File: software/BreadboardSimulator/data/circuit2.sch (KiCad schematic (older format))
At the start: 8 parts, among them Q1 Transistor, U1-8 8pinChip

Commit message: modify scale of prefabs
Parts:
- added GND, GND1, GND2, GND3: GND, symbol SchemaBoard_Library:GND
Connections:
- net GND: now also GND.1 (GND), GND1.1 (GND), GND2.1 (GND), GND3.1 (GND)
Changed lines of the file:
@@
 $EndComp
 $Comp
-L SchemaBoard_Library:GND #PWR0101
+L SchemaBoard_Library:GND GND2
 U 1 1 5D3D0435
 P 5050 5700
-F 0 "#PWR0101" H 5050 5450 50  0001 C CNN
+F 0 "GND2" H 5050 5450 50  0001 C CNN
 F 1 "GND" H 5055 5527 50  0000 C CNN
 F 2 "" H 5050 5700 50  0001 C CNN
@@
 $EndComp
 $Comp
-L SchemaBoard_Library:GND #PWR0102
+L SchemaBoard_Library:GND GND
 U 1 1 5D3D0965
 P 7900 2100
-F 0 "#PWR0102" H 7900 1850 50  0001 C CNN
+F 0 "GND" H 7900 1850 50  0001 C CNN
 F 1 "GND" H 7905 1927 50  0000 C CNN
 F 2 "" H 7900 2100 50  0001 C CNN
@@
 	5050 4700 5050 5700
 $Comp
-L SchemaBoard_Library:GND #PWR0103
+L SchemaBoard_Library:GND GND1
 U 1 1 5D3F22A2
 P 6350 5700
-F 0 "#PWR0103" H 6350 5450 50  0001 C CNN
+F 0 "GND1" H 6350 5450 50  0001 C CNN
 F 1 "GND" H 6355 5527 50  0000 C CNN
 F 2 "" H 6350 5700 50  0001 C CNN
@@
 	6350 5000 6350 5700
 $Comp
-L SchemaBoard_Library:GND #PWR0104
+L SchemaBoard_Library:GND GND3
 U 1 1 5D3FA6A0
 P 4500 6950
-F 0 "#PWR0104" H 4500 6700 50  0001 C CNN
+F 0 "GND3" H 4500 6700 50  0001 C CNN
 F 1 "GND" H 4505 6777 50  0000 C CNN
 F 2 "" H 4500 6950 50  0001 C CNN

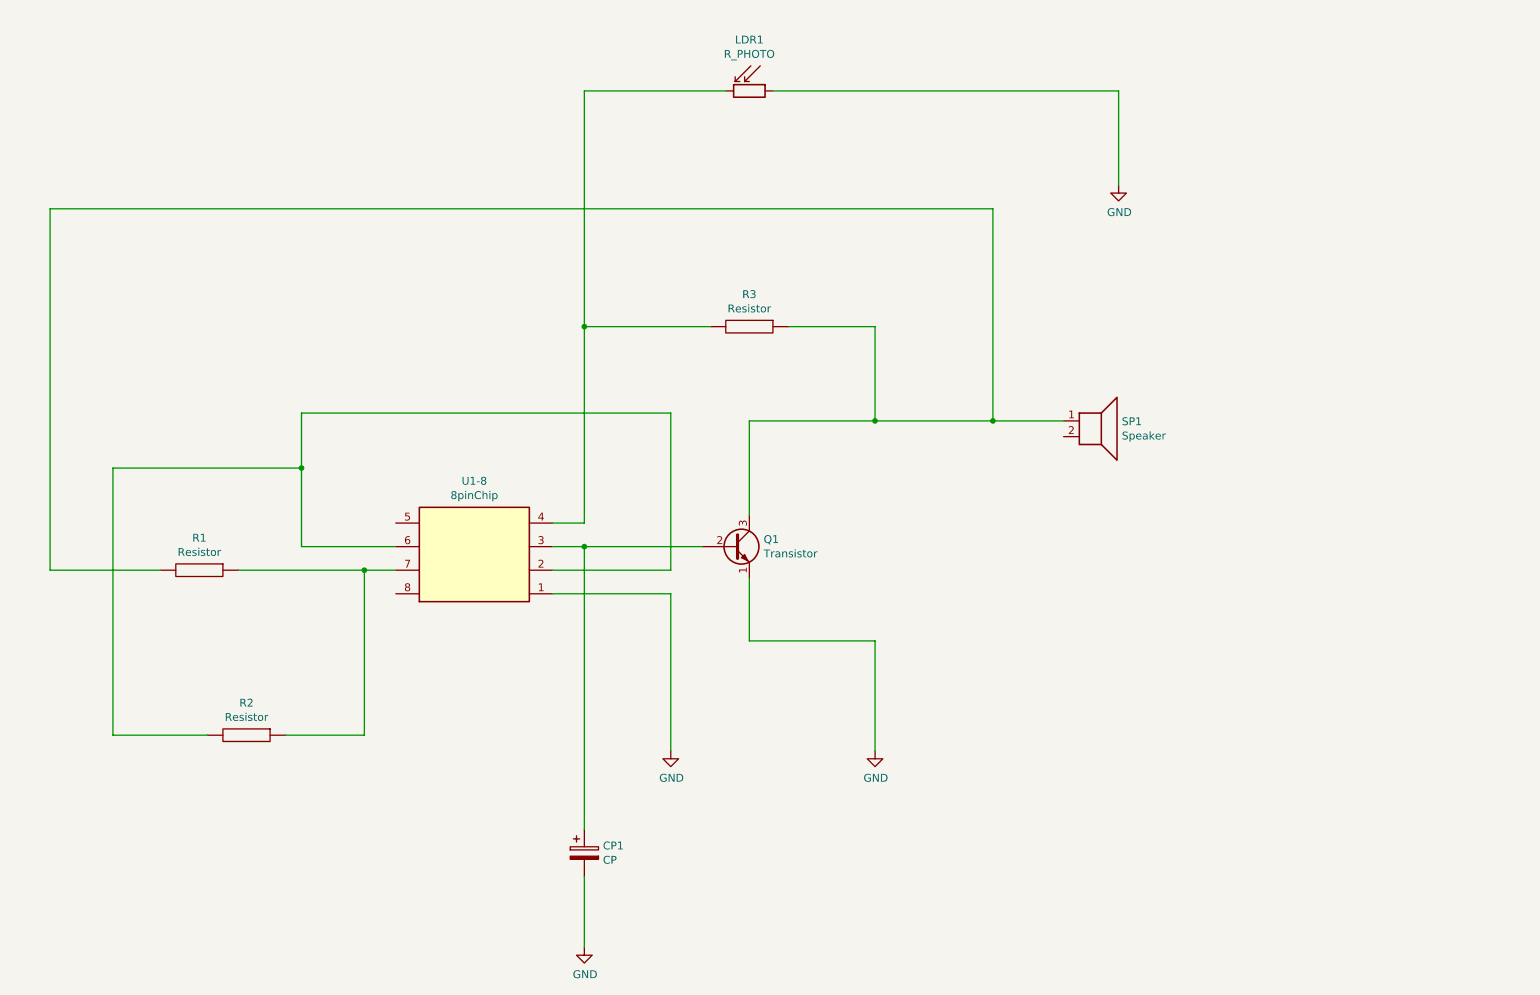
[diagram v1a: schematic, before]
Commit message: resize button for prefabs
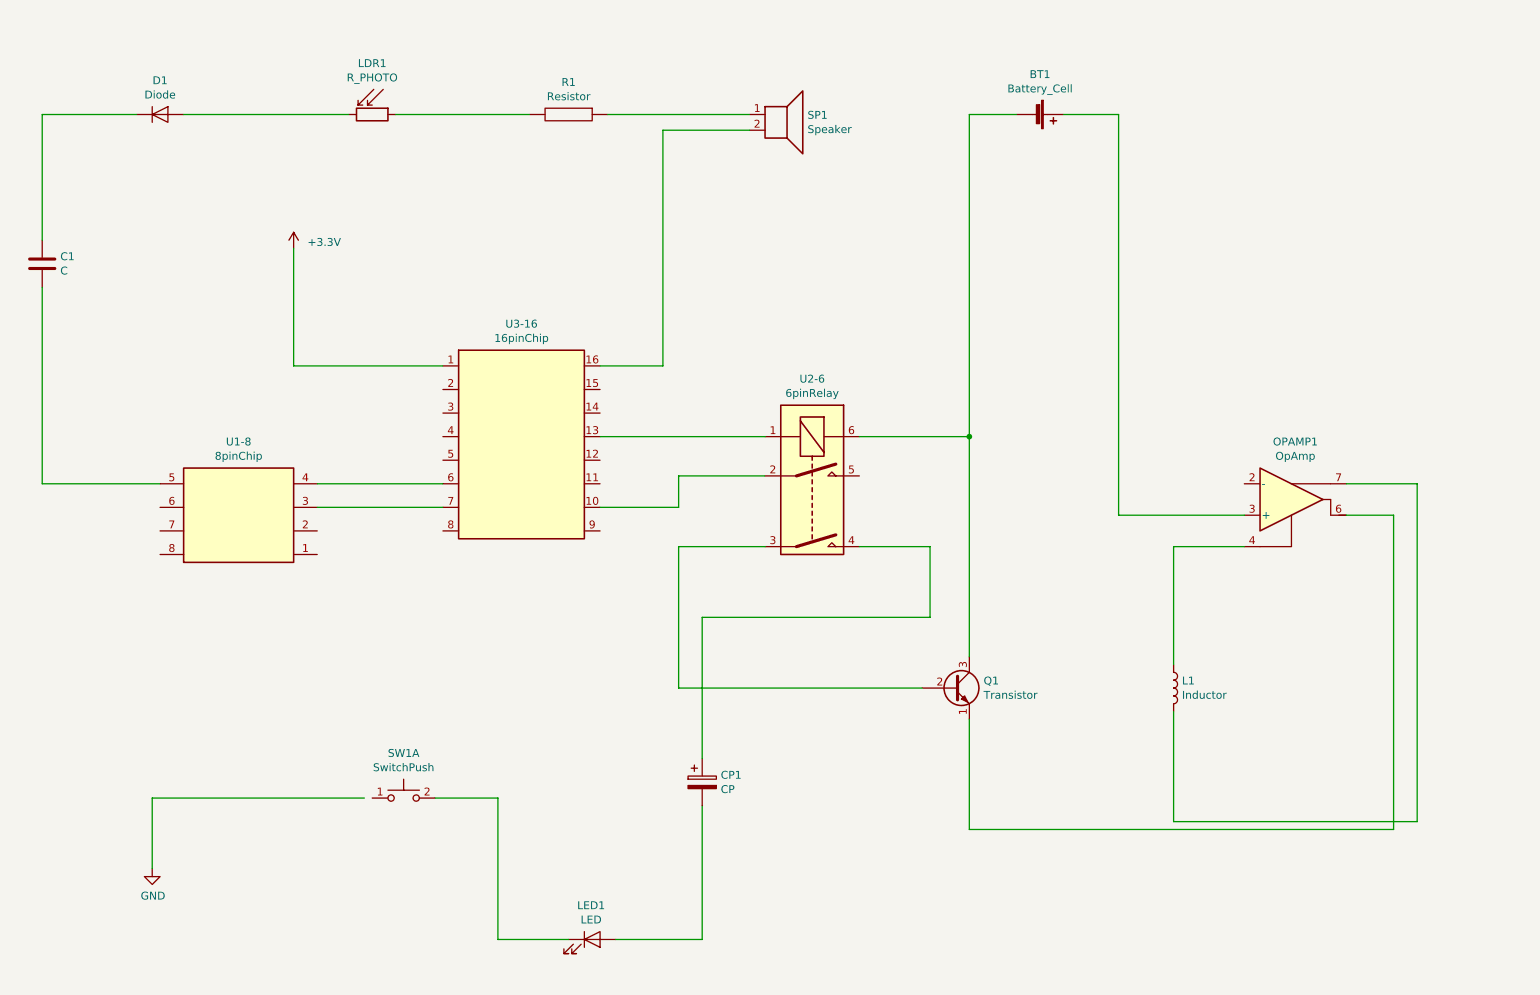
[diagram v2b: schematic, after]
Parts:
- removed GND1, GND2, GND3: GND, symbol SchemaBoard_Library:GND
- removed R1, R2: Resistor, symbol SchemaBoard_Library:Resistor
- added BT1: Battery_Cell, symbol SchemaBoard_Library:Battery_Cell
- added C1: C, symbol SchemaBoard_Library:C
- added D1: Diode, symbol SchemaBoard_Library:Diode
- added L1: Inductor, symbol SchemaBoard_Library:Inductor
- added LED1: LED, symbol SchemaBoard_Library:LED
- added OPAMP1: OpAmp, symbol SchemaBoard_Library:OpAmp
- added PWR1: +3.3V, symbol SchemaBoard_Library:+3.3V
- added SW1: SwitchPush, symbol SchemaBoard_Library:SwitchPush
- added U2-6: 6pinRelay, Relay_THT, symbol SchemaBoard_Library:6pinRelay
- added U3-16: 16pinChip, symbol SchemaBoard_Library:16pinChip
- renumbered GND to GND1, R3 to R1
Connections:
- net GND: no longer CP1.2, LDR1.1, Q1.1 (E), U1-8.1
- net at U1-8.2: no longer U1-8.6
- net at U1-8.5: now also C1.2
- net at R1.1, SP1.1: no longer Q1.3 (C)
- net at SP1.2: now also U3-16.16
- new net: U1-8.3, U3-16.7
- new net: U1-8.4, U3-16.6
- new net: LDR1.1, R1.2
- new net: D1.2 (A), LDR1.2
- new net: OPAMP1.6, Q1.1 (E)
- new net: Q1.2 (B), U2-6.3
- new net: BT1.2 (-), Q1.3 (C), U2-6.6
- new net: U2-6.1, U3-16.13
- new net: U2-6.2, U3-16.10
- new net: CP1.1, U2-6.4
- new net: C1.1, D1.1 (K)
- new net: L1.1, OPAMP1.4
- new net: L1.2, OPAMP1.7
- new net: LED1.1 (K), SW1.2 (D)
- new net: CP1.2, LED1.2 (A)
- new net: BT1.1 (+), OPAMP1.3 (+)
- new net +3V3: PWR1.1 (+3V3), U3-16.1
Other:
- moved on the sheet: CP1, LDR1, Q1, R1, SP1, U1-8

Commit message: Recover initial position if the user changes mode with disconnected components
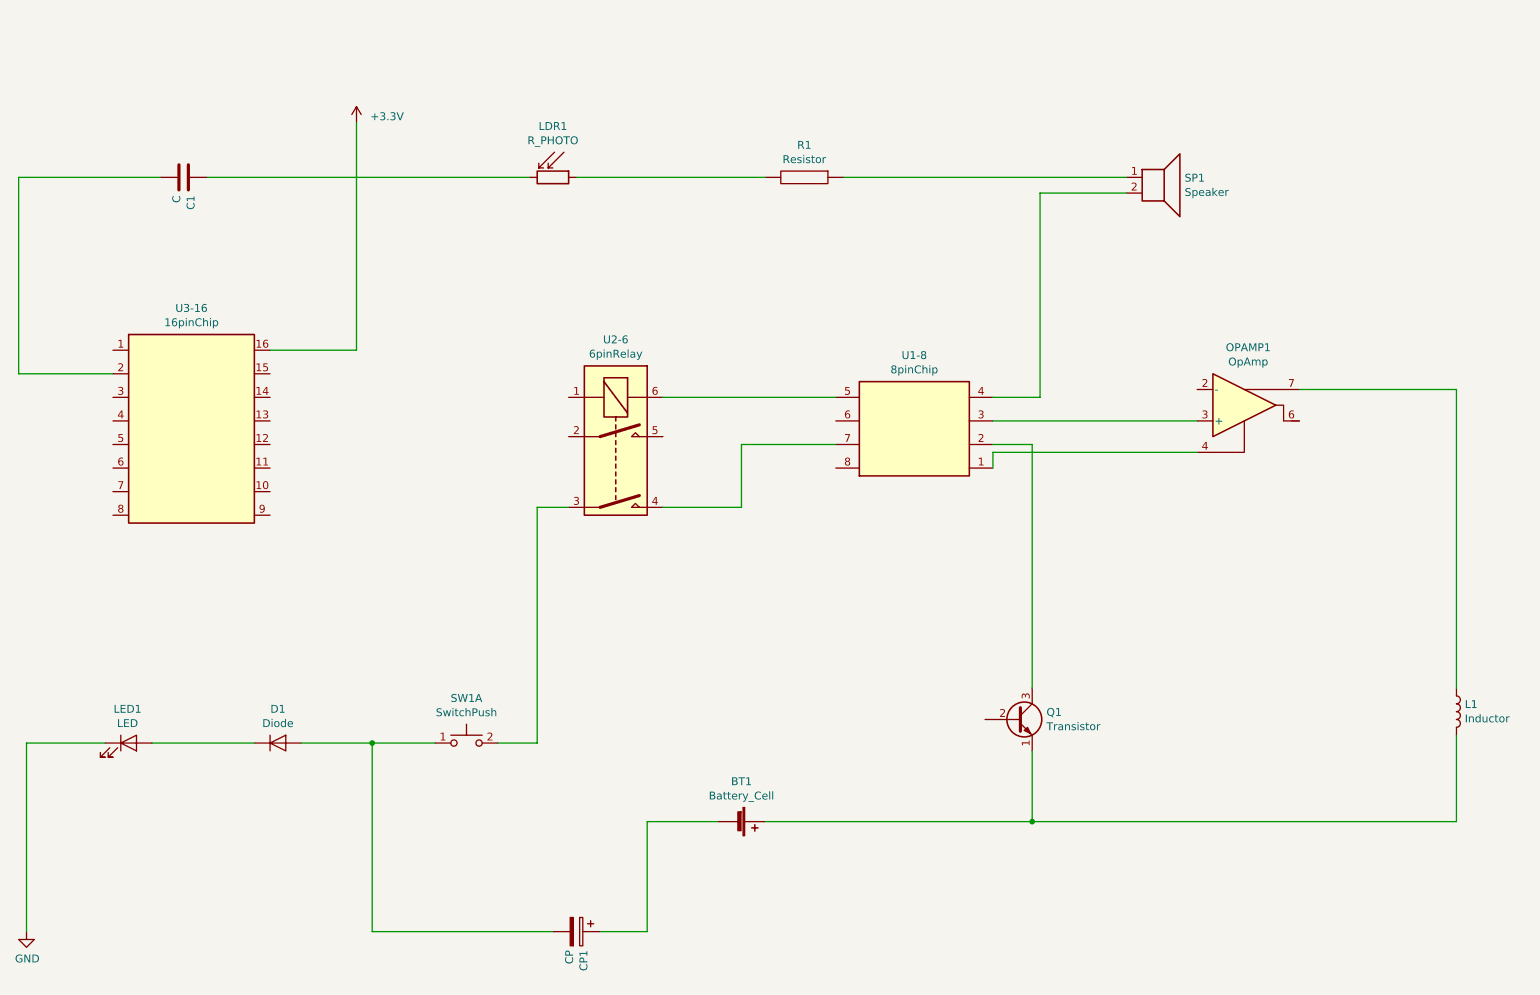
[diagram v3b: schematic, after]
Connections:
- net +3V3: now also U3-16.16; no longer U3-16.1
- net GND: now also LED1.1 (K)
- net at U1-8.1: now also OPAMP1.4
- net at U1-8.2: now also Q1.3 (C)
- net at U1-8.3: now also OPAMP1.3 (+); no longer U3-16.7
- net at U1-8.4: now also SP1.2; no longer U3-16.6
- net at U1-8.5: now also U2-6.6; no longer C1.2
- net at U1-8.7: now also U2-6.4
- net at LDR1.2: now also C1.1; no longer D1.2 (A)
- net at Q1.1 (E): now also BT1.1 (+), L1.2; no longer OPAMP1.6
- net at Q1.2 (B): no longer U2-6.3
- net at U2-6.1: no longer U3-16.13
- net at U2-6.2: no longer U3-16.10
- net at CP1.1: now also BT1.2 (-); no longer U2-6.4
- net at U3-16.2: now also C1.2
- net at D1.1 (K): now also LED1.2 (A); no longer C1.1
- net at L1.1: now also OPAMP1.7; no longer OPAMP1.4
- net at SW1.2 (D): now also U2-6.3; no longer LED1.1 (K)
- net at CP1.2: now also D1.2 (A), SW1.1 (C); no longer LED1.2 (A)
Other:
- moved on the sheet: BT1, C1, CP1, D1, L1, LDR1, LED1, OPAMP1, Q1, R1, SP1, SW1A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

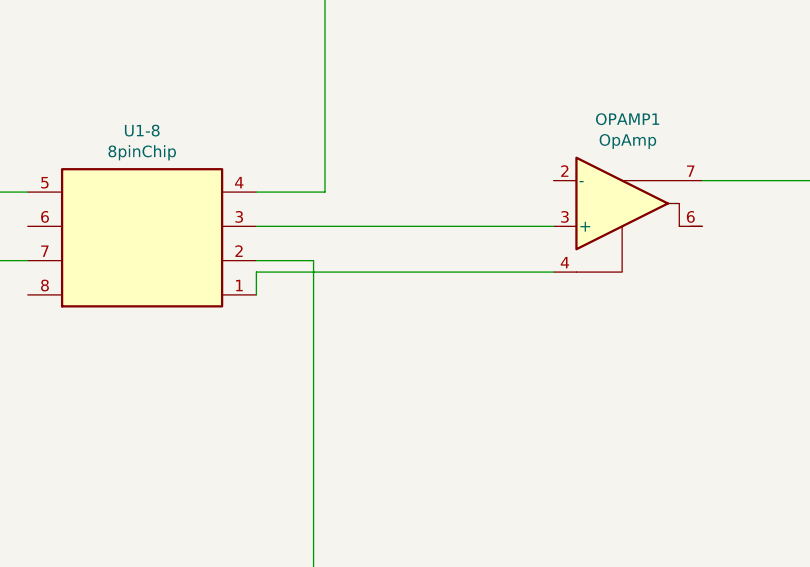
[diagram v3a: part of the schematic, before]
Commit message: Bugfix change glow icons according to mode (fritzing/schematic)
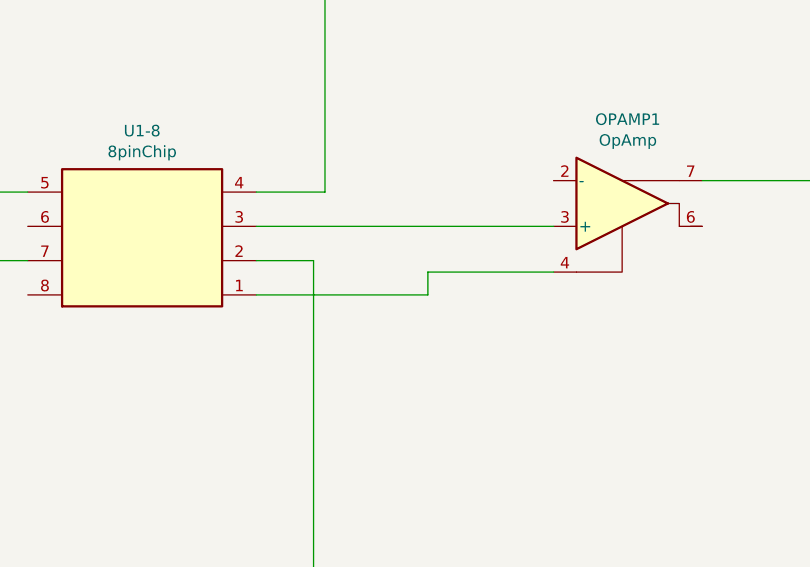
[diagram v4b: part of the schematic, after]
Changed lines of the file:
@@
 	4200 5650 3950 5650
-Wire Wire Line
-	8400 3800 7100 3800
-Wire Wire Line
-	7100 3800 7100 3900
 Wire Wire Line
 	2700 5650 3150 5650
@@
 Wire Wire Line
 	950  5650 950  6850
+Wire Wire Line
+	7100 3900 7850 3900
+Wire Wire Line
+	7850 3900 7850 3800
+Wire Wire Line
+	7850 3800 8400 3800
 $EndSCHEMATC

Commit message: In progress: travel net lists
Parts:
- removed U1-8: 8pinChip, symbol SchemaBoard_Library:8pinChip
- removed U2-6: 6pinRelay, Relay_THT, symbol SchemaBoard_Library:6pinRelay
- added GND2: GND, symbol SchemaBoard_Library:GND
- added PWR2: +3.3V, symbol SchemaBoard_Library:+3.3V
- renumbered D1 to D3, LDR1 to LDR2
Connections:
- net +3V3: now also C1.1, D3.1 (K), LDR2.2, LED1.2 (A), PWR2.1 (+3V3); no longer U3-16.16
- net GND: now also C1.2, GND2.1 (GND)
- net at OPAMP1.4: now also U3-16.12
- net at Q1.3 (C): now also U3-16.13
- net at OPAMP1.3 (+): now also U3-16.14
- net at SP1.2: now also U3-16.15
- net at SW1.2 (D): now also U3-16.6
- net at U3-16.2: no longer C1.2
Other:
- moved on the sheet: U3-16
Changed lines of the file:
@@
 L SchemaBoard_Library:+3.3V PWR1
 U 1 1 5D3E25B9
-P 3050 1700
-F 0 "PWR1" H 3050 1550 50  0001 C CNN
-F 1 "+3.3V" H 3138 1737 50  0000 L CNN
-F 2 "" H 3050 1700 50  0001 C CNN
-F 3 "" H 3050 1700 50  0001 C CNN
-	1    3050 1700
-	1    0    0    -1
-$EndComp
-$Comp
-L SchemaBoard_Library:R_PHOTO LDR1
+P 2900 1100
+F 0 "PWR1" H 2900 950 50  0001 C CNN
+F 1 "+3.3V" H 2988 1137 50  0000 L CNN
+F 2 "" H 2900 1100 50  0001 C CNN
+F 3 "" H 2900 1100 50  0001 C CNN
+	1    2900 1100
+	1    0    0    -1
+$EndComp
+$Comp
+L SchemaBoard_Library:R_PHOTO LDR2
 U 1 1 5D3CE114
 P 4300 2050
-F 0 "LDR1" V 3975 2050 50  0000 C CNN
+F 0 "LDR2" V 3975 2050 50  0000 C CNN
 F 1 "R_PHOTO" V 4066 2050 50  0000 C CNN
 F 2 "" V 4350 1800 50  0001 L CNN
@@
 $EndComp
 $Comp
-L SchemaBoard_Library:6pinRelay U2-6
-U 1 1 5D3E2F18
-P 4700 3750
-F 0 "U2-6" V 4033 3750 50  0000 C CNN
-F 1 "6pinRelay" V 4124 3750 50  0000 C CNN
-F 2 "Relay_THT" H 5200 3650 50  0001 L CNN
-F 3 "https://standexelectronics.com/wp-content/uploads/datasheet_reed_relay_DIP.pdf" H 4600 3750 50  0001 C CNN
-	1    4700 3750
-	0    1    1    0
-$EndComp
-$Comp
-L SchemaBoard_Library:8pinChip U1-8
-U 1 1 5D3CCD89
-P 6600 3650
-F 0 "U1-8" H 6600 4117 50  0000 C CNN
-F 1 "8pinChip" H 6600 4026 50  0000 C CNN
-F 2 "" H 6600 3650 50  0001 C CNN
-F 3 "http://www.ti.com/lit/ds/symlink/lm555.pdf" H 6600 3650 50  0001 C CNN
-	1    6600 3650
-	1    0    0    -1
-$EndComp
-$Comp
 L SchemaBoard_Library:16pinChip U3-16
 U 1 1 5D3E3E98
-P 2000 3650
-F 0 "U3-16" H 2000 4417 50  0000 C CNN
-F 1 "16pinChip" H 2000 4326 50  0000 C CNN
-F 2 "" H 2000 3250 50  0001 C CNN
-F 3 "" H 2000 3250 50  0001 C CNN
-	1    2000 3650
-	1    0    0    -1
-$EndComp
-$Comp
-L SchemaBoard_Library:Diode D1
+P 6600 3800
+F 0 "U3-16" H 6600 4567 50  0000 C CNN
+F 1 "16pinChip" H 6600 4476 50  0000 C CNN
+F 2 "" H 6600 3400 50  0001 C CNN
+F 3 "" H 6600 3400 50  0001 C CNN
+	1    6600 3800
+	1    0    0    -1
+$EndComp
+$Comp
+L SchemaBoard_Library:Diode D3
 U 1 1 5D3E50B4
 P 2550 5650
-F 0 "D1" H 2550 5866 50  0000 C CNN
+F 0 "D3" H 2550 5866 50  0000 C CNN
 F 1 "Diode" H 2550 5775 50  0000 C CNN
 F 2 "" H 2550 5650 50  0001 C CNN
@@
 $EndComp
 Wire Wire Line
-	3050 1700 3050 3150
-Wire Wire Line
-	3050 3150 2500 3150
-Wire Wire Line
-	2100 2050 4150 2050
+	2100 2050 2900 2050
 Wire Wire Line
 	4450 2050 5650 2050
 Wire Wire Line
-	1800 2050 900  2050
-Wire Wire Line
-	900  2050 900  3300
-Wire Wire Line
-	900  3300 1500 3300
+	1800 2050 950  2050
 Wire Wire Line
 	6150 2050 7950 2050
@@
 	7350 3750 7350 5300
 Wire Wire Line
-	5000 3450 6100 3450
-Wire Wire Line
-	6100 3750 5500 3750
-Wire Wire Line
-	5500 3750 5500 4150
-Wire Wire Line
-	5500 4150 5000 4150
-Wire Wire Line
-	4400 4150 4200 4150
-Wire Wire Line
-	4200 4150 4200 5650
-Wire Wire Line
 	4200 5650 3950 5650
 Wire Wire Line
 	2700 5650 3150 5650
 Wire Wire Line
-	1750 5650 2400 5650
+	1750 5650 2000 5650
 Wire Wire Line
 	5650 6150 7350 6150
@@
 Wire Wire Line
 	7850 3800 8400 3800
+Wire Wire Line
+	6100 4050 4200 4050
+Wire Wire Line
+	4200 4050 4200 5650
+$Comp
+L SchemaBoard_Library:GND GND2
+U 1 1 5D45597B
+P 950 3650
+F 0 "GND2" H 950 3400 50  0001 C CNN
+F 1 "GND" H 955 3477 50  0000 C CNN
+F 2 "" H 950 3650 50  0001 C CNN
+F 3 "" H 950 3650 50  0001 C CNN
+	1    950  3650
+	1    0    0    -1
+$EndComp
+Wire Wire Line
+	950  3650 950  2050
+Wire Wire Line
+	2900 1100 2900 2050
+Connection ~ 2900 2050
+Wire Wire Line
+	2900 2050 4150 2050
+$Comp
+L SchemaBoard_Library:+3.3V PWR2
+U 1 1 5D4586B3
+P 2000 3800
+F 0 "PWR2" H 2000 3650 50  0001 C CNN
+F 1 "+3.3V" H 2088 3837 50  0000 L CNN
+F 2 "" H 2000 3800 50  0001 C CNN
+F 3 "" H 2000 3800 50  0001 C CNN
+	1    2000 3800
+	1    0    0    -1
+$EndComp
+Wire Wire Line
+	2000 3800 2000 5650
+Connection ~ 2000 5650
+Wire Wire Line
+	2000 5650 2400 5650
 $EndSCHEMATC
